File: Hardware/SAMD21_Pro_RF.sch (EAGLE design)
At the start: 62 parts, among them J10 AVR_SPI_PROG_3X2TESTPOINTS, J12 JST, J13 U.FL, J7 PTH, J9 External On/Off, U1 MCP73831, U2 915MHz, U4 ATSAMD21G, U5 4MB Flash, U6 3.3V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

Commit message: Added Sparkfun labels, correct RFM module (same pinout), fixed silk
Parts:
- removed JP1, JP2: JUMPER-SMT_2_NO_SILK, SparkFun-Jumpers:JUMPER-SMT_2_NO_SILK
- removed U$34: SPARKX-LOGO2, SparkX:SPARKX-LOGO2
- removed U2: 915MHz, SparkFun-RF:RFM69HCW-915
- added JP3, JP4: JUMPER-SMT_2_NO_SILK, SparkFun-Jumpers:JUMPER-SMT_2_NO_SILK
- added LOGO2: SFE_LOGO_NAME.1_INCH, SparkFun-Aesthetics:SFE_LOGO_NAME.1_INCH
- added U3: RFM96W, SparkX:RFM96W
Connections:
- removed net D10: JP1.2, U4.PA18(SER1:2+)_D10
- removed net D11: JP2.2, U4.PA16(I2C/SER1:0+)_D11
- removed net RFM_IO1: JP1.1, U2.IO1
- removed net RFM_IO2: JP2.1, U2.IO2
- new net D10_LORA-WAN: JP3.2, U4.PA18(SER1:2+)_D10
- new net D11_LORA-WAN: JP4.2, U4.PA16(I2C/SER1:0+)_D11
- new net N$17: JP3.1, U3.DIO1
- new net N$18: JP4.1, U3.DIO2
- net !RFM_CS: now also U3.NSS; no longer U2.!CS
- net 3.3V: now also U3.3.3V; no longer U2.VCC
- net ANT: now also U3.ANT; no longer U2.ANT
- net GND: now also U3.GND; no longer U2.GND
- net MISO: now also U3.MISO; no longer U2.MISO
- net MOSI: now also U3.MOSI; no longer U2.MOSI
- net RFM_INT: now also U3.DIO0; no longer U2.IO0/INT
- net RFM_RST: now also U3.!RESET; no longer U2.RST
- net SCK: now also U3.SCK; no longer U2.SCK
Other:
- note added: "RFM96W"
- note removed: "RFM69HCW-915"
- note removed: "look up interrupt"
- moved on the sheet: R4

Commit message: Removed Flash, added standoffs
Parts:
- removed J10: AVR_SPI_PROG_3X2TESTPOINTS, SparkFun-Connectors:AVR_SPI_PROG_3X2TESTPOINTS
- removed R8: 10k, SparkFun-Resistors:10KOHM-0603-1/10W-1%
- removed U5: 4MB Flash, SparkFun-IC-Memory:AT25SF041
- added H1, H2: STAND-OFFTIGHT, SparkFun-Hardware:STAND-OFFTIGHT
- added TP1, TP2: TEST-POINT3, SparkFun-Connectors:TEST-POINT3
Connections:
- net !RST: no longer J10.5
- net 3.3V: no longer J10.2, R8.2, U5.!HOLD(D3), U5.!WP(D2), U5.VCC
- net D8_!FLASH_CS: no longer R8.1, U5.!CS
- net GND: no longer J10.6, U5.GND
- net MISO: no longer J10.1, U5.SO(D1)
- net MOSI: no longer U5.SI(D0)
- net SCK: no longer U5.SCK
- net SWDCLK: now also TP2.1; no longer J10.3
- net SWDIO: now also TP1.1; no longer J10.4
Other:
- note added: "TEST POINTS"
- note removed: "FLASH MEMORY"
- note removed: "PROGRAMMING HEADER"
- moved on the sheet: C2, C3, D1, D2, D6, J1, J11, J2, J3, J4, J5, J6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

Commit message: Post-checklist
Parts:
- U4: device temp:ATSAMD21G -> SparkFun-IC-Microcontroller:ATSAMD21G
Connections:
- net RFM_RST renamed !RFM_RST
- removed net D8_!FLASH_CS: U4.D8_PA06(AIN6/SER0:2/TC1:0)
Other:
- note added: "RX/TX and STAT LEDs"
- note removed: "RX/TX LEDs"
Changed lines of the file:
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@@
 <part name="J13" library="SparkFun-Connectors" deviceset="U.FL" device="" value="U.FL"/>
 <part name="GND3" library="supply1" library_urn="urn:adsk.eagle:library:371" deviceset="GND" device=""/>
-<part name="U4" library="temp" deviceset="ATSAMD21G" device=""/>
+<part name="U4" library="SparkFun-IC-Microcontroller" deviceset="ATSAMD21G" device=""/>
 <part name="C4" library="SparkFun-Capacitors" deviceset="0.1UF" device="-0603-25V-(+80/-20%)" value="0.1uF"/>
 <part name="GND6" library="supply1" library_urn="urn:adsk.eagle:library:371" deviceset="GND" device=""/>
@@
 <wire x1="370.84" y1="175.26" x2="370.84" y2="218.44" width="0.2032" layer="97" style="shortdash"/>
 <wire x1="370.84" y1="218.44" x2="431.8" y2="218.44" width="0.2032" layer="97" style="shortdash"/>
-<text x="375.92" y="213.36" size="2.54" layer="94">Antenna</text>
+<text x="375.92" y="213.36" size="2.54" layer="94" font="vector">Antenna</text>
 <wire x1="71.12" y1="83.82" x2="71.12" y2="0" width="0.2032" layer="97" style="shortdash"/>
-<text x="76.2" y="78.74" size="2.54" layer="94" font="vector">RX/TX LEDs</text>
+<text x="76.2" y="78.74" size="2.54" layer="94" font="vector">RX/TX and STAT LEDs</text>
 <wire x1="114.3" y1="144.78" x2="116.84" y2="144.78" width="0.2032" layer="97" style="shortdash"/>
 <wire x1="116.84" y1="144.78" x2="116.84" y2="172.72" width="0.2032" layer="97" style="shortdash"/>
@@
 <instance part="R2" gate="G$1" x="190.5" y="220.98" rot="R90"/>
 <instance part="GND9" gate="1" x="190.5" y="210.82"/>
-<instance part="U$26" gate="G$1" x="325.628" y="48.26"/>
+<instance part="U$26" gate="G$1" x="406.908" y="53.34"/>
 <instance part="R4" gate="G$1" x="365.76" y="236.22" rot="R90"/>
 <instance part="P+7" gate="G$1" x="365.76" y="243.84"/>
@@
 <instance part="J13" gate="G$1" x="401.32" y="198.12" rot="R180"/>
 <instance part="GND3" gate="1" x="406.4" y="190.5"/>
-<instance part="U4" gate="G$1" x="96.52" y="228.6"/>
+<instance part="U4" gate="G$1" x="93.98" y="220.98"/>
 <instance part="C4" gate="G$1" x="76.2" y="114.3" smashed="yes" rot="R180">
 <attribute name="NAME" x="77.216" y="114.427" size="1.778" layer="95" font="vector"/>
@@
 <wire x1="132.08" y1="264.16" x2="132.08" y2="266.7" width="0.1524" layer="91"/>
 <pinref part="P+9" gate="G$1" pin="3.3V"/>
-<wire x1="129.54" y1="261.62" x2="132.08" y2="261.62" width="0.1524" layer="91"/>
 <wire x1="132.08" y1="261.62" x2="132.08" y2="264.16" width="0.1524" layer="91"/>
 <junction x="132.08" y="264.16"/>
 <pinref part="U4" gate="G$1" pin="VDDIO@17"/>
 <pinref part="U4" gate="G$1" pin="VDDIO@36"/>
+<wire x1="132.08" y1="261.62" x2="129.54" y2="261.62" width="0.1524" layer="91"/>
 </segment>
 <segment>
@@
 <pinref part="J13" gate="G$1" pin="SIGNAL"/>
 <wire x1="393.7" y1="198.12" x2="396.24" y2="198.12" width="0.1524" layer="91"/>
-<label x="393.7" y="198.12" size="1.27" layer="95" rot="R180" xref="yes"/>
+<label x="393.7" y="198.12" size="1.27" layer="95" font="vector" rot="R180" xref="yes"/>
 </segment>
 <segment>
 <wire x1="408.94" y1="127" x2="406.4" y2="127" width="0.1524" layer="91"/>
 <pinref part="J4" gate="G$1" pin="1"/>
-<label x="406.4" y="127" size="1.27" layer="95" rot="R180" xref="yes"/>
+<label x="406.4" y="127" size="1.27" layer="95" font="vector" rot="R180" xref="yes"/>
 </segment>
 <segment>
@@
 </segment>
 </net>
-<net name="RFM_RST" class="0">
+<net name="!RFM_RST" class="0">
 <segment>
 <pinref part="U4" gate="G$1" pin="PA21(SER5:3+)_D7"/>
 <wire x1="129.54" y1="223.52" x2="132.08" y2="223.52" width="0.1524" layer="91"/>
-<label x="132.08" y="223.52" size="1.27" layer="95" xref="yes"/>
+<label x="132.08" y="223.52" size="1.27" layer="95" font="vector" xref="yes"/>
 </segment>
 <segment>
@@
 <pinref part="J3" gate="G$1" pin="8"/>
 <wire x1="317.5" y1="142.24" x2="320.04" y2="142.24" width="0.1524" layer="91"/>
-<label x="317.5" y="142.24" size="1.27" layer="95" rot="R180" xref="yes"/>
+<label x="317.5" y="142.24" size="1.27" layer="95" font="vector" rot="R180" xref="yes"/>
 </segment>
 <segment>
@@
 </segment>
 </net>
-<net name="D8_!FLASH_CS" class="0">
-<segment>
-<wire x1="60.96" y1="218.44" x2="58.42" y2="218.44" width="0.1524" layer="91"/>
-<label x="58.42" y="218.44" size="1.27" layer="95" font="vector" rot="R180" xref="yes"/>
-<pinref part="U4" gate="G$1" pin="D8_PA06(AIN6/SER0:2/TC1:0)"/>
-</segment>
-</net>
 <net name="MOSI" class="0">
 <segment>
@@
 <pinref part="U4" gate="G$1" pin="PA17(I2C/SER1:1+)_D13"/>
 <wire x1="129.54" y1="233.68" x2="132.08" y2="233.68" width="0.1524" layer="91"/>
-<label x="132.08" y="233.68" size="1.27" layer="95" xref="yes"/>
+<label x="132.08" y="233.68" size="1.27" layer="95" font="vector" xref="yes"/>
 </segment>
 <segment>
@@
 <wire x1="132.08" y1="58.42" x2="132.08" y2="60.96" width="0.1524" layer="91"/>
 <wire x1="132.08" y1="60.96" x2="134.62" y2="60.96" width="0.1524" layer="91"/>
-<label x="134.62" y="60.96" size="1.27" layer="95" xref="yes"/>
-</segment>
-</net>
+<label x="134.62" y="60.96" size="1.27" layer="95" font="vector" xref="yes"/>
+</segment>
+</net>

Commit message: Post Review fixes
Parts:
- U3: value RFM96W -> RFM95W; device SparkX:RFM96W -> SparkFun-RF:RFM95W
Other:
- note added: "RFM95W"
- note removed: "RFM96W"
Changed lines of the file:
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@@
 <part name="R3" library="SparkFun-Resistors" deviceset="1KOHM" device="-0603-1/10W-1%" value="1k"/>
 <part name="GND21" library="SparkFun" deviceset="GND" device=""/>
-<part name="U3" library="SparkX" deviceset="RFM96W" device=""/>
+<part name="U3" library="SparkFun-RF" deviceset="RFM95W" device=""/>
 <part name="JP3" library="SparkFun-Jumpers" deviceset="JUMPER-SMT_2_NO" device="_SILK" value=""/>
 <part name="JP4" library="SparkFun-Jumpers" deviceset="JUMPER-SMT_2_NO" device="_SILK" value=""/>
@@
 <wire x1="299.72" y1="175.26" x2="370.84" y2="175.26" width="0.2032" layer="97" style="shortdash"/>
 <wire x1="370.84" y1="175.26" x2="431.8" y2="175.26" width="0.2032" layer="97" style="shortdash"/>
-<text x="304.8" y="271.78" size="2.54" layer="94" font="vector">RFM96W</text>
+<text x="304.8" y="271.78" size="2.54" layer="94" font="vector">RFM95W</text>
 <wire x1="0" y1="187.96" x2="27.94" y2="187.96" width="0.2032" layer="97" style="shortdash"/>
 <wire x1="27.94" y1="187.96" x2="27.94" y2="243.84" width="0.2032" layer="97" style="shortdash"/>
@@
 <instance part="U3" gate="G$1" x="335.28" y="241.3"/>
 <instance part="JP3" gate="G$1" x="375.92" y="254" smashed="yes">
-<attribute name="NAME" x="369.316" y="254.508" size="1.778" layer="95" font="vector"/>
+<attribute name="NAME" x="373.634" y="255.778" size="1.778" layer="95" font="vector"/>
 <attribute name="VALUE" x="373.38" y="251.46" size="1.778" layer="96" font="vector" align="top-left"/>
 </instance>
 <instance part="JP4" gate="G$1" x="375.92" y="251.46" smashed="yes">
-<attribute name="NAME" x="369.316" y="251.968" size="1.778" layer="95" font="vector"/>
+<attribute name="NAME" x="373.634" y="247.65" size="1.778" layer="95" font="vector"/>
 <attribute name="VALUE" x="373.38" y="248.92" size="1.778" layer="96" font="vector" align="top-left"/>
 </instance>
@@
 </segment>
 <segment>
-<wire x1="180.34" y1="243.84" x2="190.5" y2="243.84" width="0.1524" layer="91"/>
-<pinref part="J7" gate="G$1" pin="2"/>
-<label x="193.04" y="243.84" size="1.27" layer="95" font="vector" xref="yes"/>
 <pinref part="R1" gate="G$1" pin="2"/>
-<wire x1="190.5" y1="243.84" x2="193.04" y2="243.84" width="0.1524" layer="91"/>
-<wire x1="190.5" y1="241.3" x2="190.5" y2="243.84" width="0.1524" layer="91"/>
-<junction x="190.5" y="243.84"/>
 <wire x1="193.04" y1="259.08" x2="190.5" y2="259.08" width="0.1524" layer="91"/>
 <pinref part="F1" gate="F1" pin="1"/>
 <pinref part="J12" gate="G$1" pin="1"/>
 <wire x1="190.5" y1="259.08" x2="180.34" y2="259.08" width="0.1524" layer="91"/>
-<wire x1="190.5" y1="243.84" x2="190.5" y2="259.08" width="0.1524" layer="91"/>
+<wire x1="190.5" y1="241.3" x2="190.5" y2="243.84" width="0.1524" layer="91"/>
 <junction x="190.5" y="259.08"/>
+<wire x1="190.5" y1="243.84" x2="190.5" y2="248.92" width="0.1524" layer="91"/>
+<wire x1="190.5" y1="248.92" x2="190.5" y2="259.08" width="0.1524" layer="91"/>
+<wire x1="193.04" y1="248.92" x2="190.5" y2="248.92" width="0.1524" layer="91"/>
+<junction x="190.5" y="248.92"/>
+<wire x1="180.34" y1="243.84" x2="190.5" y2="243.84" width="0.1524" layer="91"/>
+<pinref part="J7" gate="G$1" pin="2"/>
+<junction x="190.5" y="243.84"/>
+<label x="193.04" y="248.92" size="1.27" layer="95" font="vector" xref="yes"/>
 </segment>
 </net>
@@
 <wire x1="215.9" y1="254" x2="220.98" y2="254" width="0.1524" layer="91"/>
 <wire x1="220.98" y1="254" x2="220.98" y2="261.62" width="0.1524" layer="91"/>
-<wire x1="220.98" y1="261.62" x2="226.06" y2="261.62" width="0.1524" layer="91"/>
+<wire x1="220.98" y1="261.62" x2="223.52" y2="261.62" width="0.1524" layer="91"/>
 <junction x="226.06" y="261.62"/>
 <junction x="220.98" y="261.62"/>
@@
 <pinref part="S1" gate="1" pin="P"/>
 <pinref part="J9" gate="G$1" pin="1"/>
-<wire x1="226.06" y1="261.62" x2="226.06" y2="264.16" width="0.1524" layer="91"/>
-<label x="226.06" y="264.16" size="1.27" layer="95" font="vector" rot="R90" xref="yes"/>
-</segment>
-<segment>
+<wire x1="223.52" y1="261.62" x2="226.06" y2="261.62" width="0.1524" layer="91"/>
+<wire x1="223.52" y1="264.16" x2="223.52" y2="261.62" width="0.1524" layer="91"/>
+<junction x="223.52" y="261.62"/>
+<label x="223.52" y="264.16" size="1.27" layer="95" font="vector" rot="R90" xref="yes"/>
+</segment>
+<segment>

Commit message: Issues caught
Replaced 10k resistors with 1M Ohm resistors, added Mosfet circuit, moved decoupling capacitors in schematic to more clearly reflect their placement on the board, and removed jumper from RAW line. All power lines have been updated with better labels.
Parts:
- removed SJ2: USB Power, SparkFun-Jumpers:JUMPER-SMT_2_NC_TRACE_SILK
- added C5: 1.0uF, SparkFun-Capacitors:1.0UF-0603-16V-10%
- added D3: BAT20J, SparkFun-DiscreteSemi:DIODE-SCHOTTKY-BAT20J
- added Q1: 2.5A/30V, SparkFun-DiscreteSemi:MOSFET-PCHANNELDMG2307L
- added R8: 10k, SparkFun-Resistors:10KOHM-0603-1/10W-1%
- R1, R2: value 10k -> 1M; device SparkFun-Resistors:10KOHM-0603-1/10W-1% -> SparkFun-Resistors:1MOHM-0603-1/4W-5%
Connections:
- removed net USB_VCC: C11.2, C9.1, D4.A, J1.VBUS, J8.2, SJ2.2, U1.VIN
- removed net VBATT: C1.+, F1.1, J12.1, J7.2, R1.2, U1.VBAT
- new net VIN: C5.1, J9.1, S1.P, U6.EN, U6.IN
- new net V_BATT: C1.+, J12.1, J7.2, Q1.D, R1.2, U1.VBAT
- new net V_USB: C11.2, C9.1, D3.A, D4.A, J1.VBUS, J8.2, Q1.G, R8.2, U1.VIN
- net GND: now also C5.2, R8.1
- net RAW: now also D3.C, F1.1, Q1.S; no longer J9.1, S1.P, SJ2.1, U6.EN, U6.IN
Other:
- note added: "Switch"
- note removed: "Cut this jumper if powering the board with more than 5.5V"
- note removed: "Decoupling"
- note removed: "VDDIN"
- moved on the sheet: C1, C10, C11, C12, C13, C14, C15, C2, C3, C4, C6, C9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

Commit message: v10
Cleanup of repo, updated readme.
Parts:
- D3: value BAT20J -> 1A/23V/620mV
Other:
- note added: "v10"
- note removed: "x01"

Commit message: VDDCORE now has 01uF cap to GND
Previously, it was incorrectly connected to VDDIN (3.3V)
-bumped version to v11
-updated gitignore
-added quiic logo
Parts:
- added C7: 0.1uF, SparkFun-Capacitors:0.1UF-0603-25V-(+80/-20%)
- added LOGO3: QWIIC_LOGO_5MM, SparkFun-Aesthetics:QWIIC_LOGO_5MM
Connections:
- new net N$4: C7.2, U4.VDDCORE
- net 3.3V: no longer U4.VDDCORE
- net GND: now also C7.1
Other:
- note added: "Pete Lewis"
- note added: "Revised by:"
- note added: "v11"
- note removed: "v10"
- moved on the sheet: C4

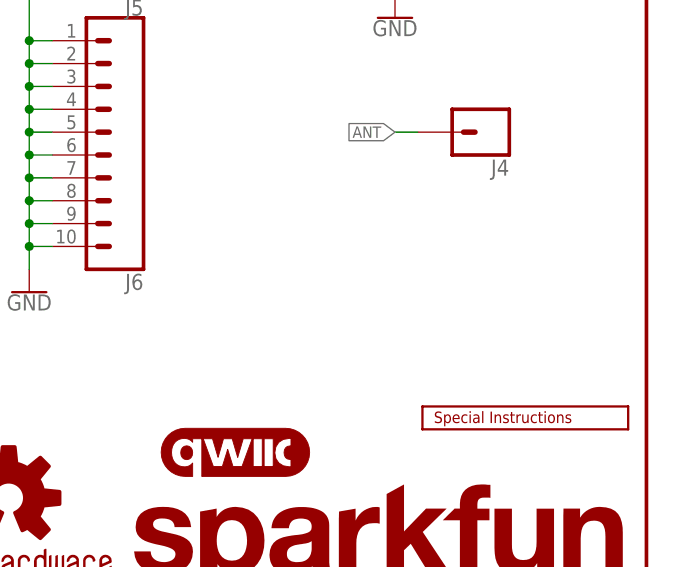
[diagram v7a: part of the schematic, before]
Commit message: included PTH headers for SWD lines
note, I did not move test points.
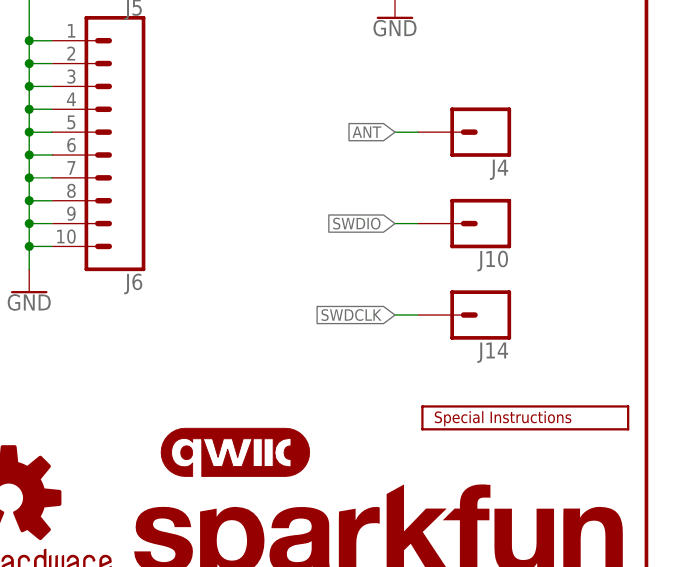
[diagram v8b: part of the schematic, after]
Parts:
- added J10, J14: (no value), SparkFun-Connectors:CONN_01PTH_NO_SILK_YES_STOP
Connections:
- net SWDCLK: now also J14.1
- net SWDIO: now also J10.1
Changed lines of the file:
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@@
 <part name="GND19" library="SparkFun-PowerSymbols" deviceset="GND" device=""/>
 <part name="LOGO3" library="SparkFun-Aesthetics" deviceset="QWIIC_LOGO" device="_5MM"/>
+<part name="J10" library="SparkFun-Connectors" deviceset="CONN_01" device="PTH_NO_SILK_YES_STOP"/>
+<part name="J14" library="SparkFun-Connectors" deviceset="CONN_01" device="PTH_NO_SILK_YES_STOP"/>
 </parts>
 <sheets>
@@
 </instance>
 <instance part="LOGO3" gate="G$1" x="386.08" y="50.8" smashed="yes"/>
+<instance part="J10" gate="G$1" x="414.02" y="76.2" smashed="yes" rot="R180">
+<attribute name="VALUE" x="416.56" y="81.026" size="1.778" layer="96" font="vector" rot="R180"/>
+<attribute name="NAME" x="416.56" y="73.152" size="1.778" layer="95" font="vector" rot="R180"/>
+</instance>
+<instance part="J14" gate="G$1" x="414.02" y="66.04" smashed="yes" rot="R180">
+<attribute name="VALUE" x="416.56" y="70.866" size="1.778" layer="96" font="vector" rot="R180"/>
+<attribute name="NAME" x="416.56" y="62.992" size="1.778" layer="95" font="vector" rot="R180"/>
+</instance>
 </instances>
 <busses>
@@
 <label x="129.54" y="109.22" size="1.27" layer="95" font="vector" rot="R180" xref="yes"/>
 </segment>
+<segment>
+<pinref part="J10" gate="G$1" pin="1"/>
+<wire x1="406.4" y1="76.2" x2="403.86" y2="76.2" width="0.1524" layer="91"/>
+<label x="403.86" y="76.2" size="1.27" layer="95" font="vector" rot="R180" xref="yes"/>
+</segment>
 </net>
 <net name="SWDCLK" class="0">
@@
 <label x="129.54" y="101.6" size="1.27" layer="95" font="vector" rot="R180" xref="yes"/>
 </segment>
-</net>
+<segment>
+<pinref part="J14" gate="G$1" pin="1"/>
+<wire x1="406.4" y1="66.04" x2="403.86" y2="66.04" width="0.1524" layer="91"/>
+<label x="403.86" y="66.04" size="1.27" layer="95" font="vector" rot="R180" xref="yes"/>
+</segment>
+</net>
